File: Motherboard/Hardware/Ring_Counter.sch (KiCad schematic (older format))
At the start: 91 parts, among them Q10 BC848, Q11 BC848, Q12 BC848, Q13 BC848, Q14 BC848, Q15 BC848, Q16 BC848, Q17 BC858, Q18 BC848, Q19 BC858, Q20 BC848, Q21 BC858, Q22 BC858, Q23 BC848, Q24 BC848, Q25 BC848, Q26 BC848, Q27 BC848, Q28 BC848, Q29 BC848, Q30 BC848, Q31 BC848, Q32 BC848, Q33 BC848, Q34 BC858, Q35 BC858, Q36 BC858, Q37 BC858, Q38 BC858, Q39 BC858, Q40 BC848, Q41 BC848, Q42 BC858, Q43 BC858, Q46 BC858

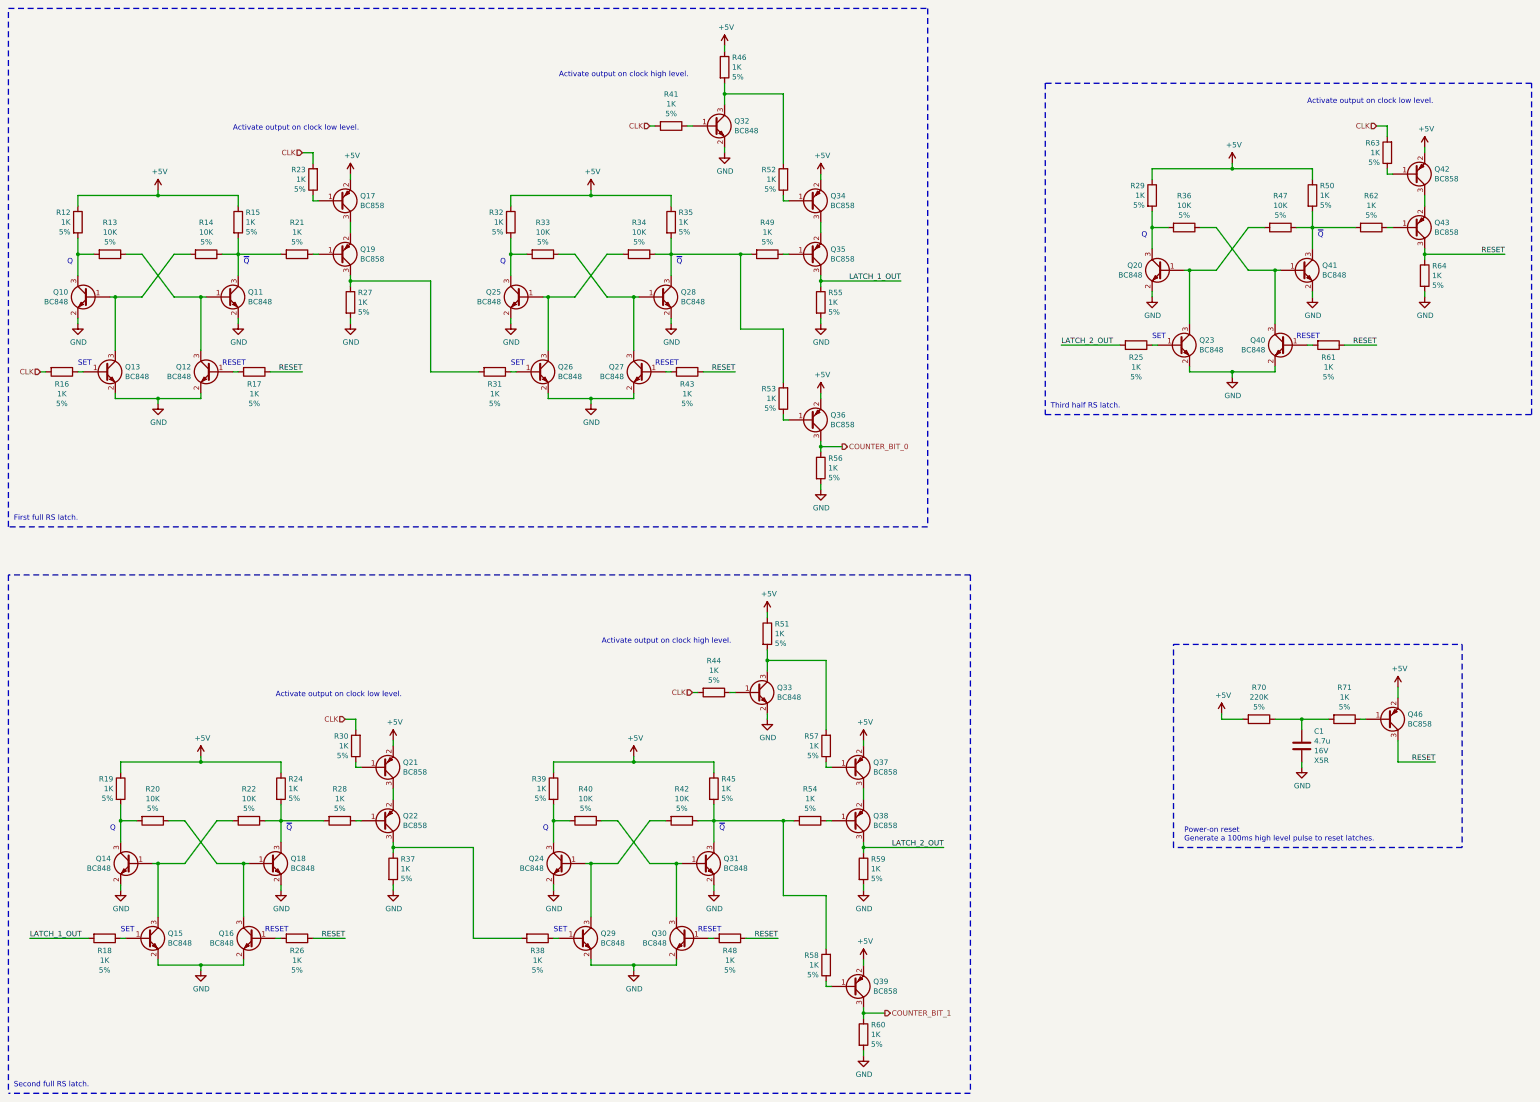
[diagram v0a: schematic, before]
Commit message: Renamed all motherboard components so the name are ordered.
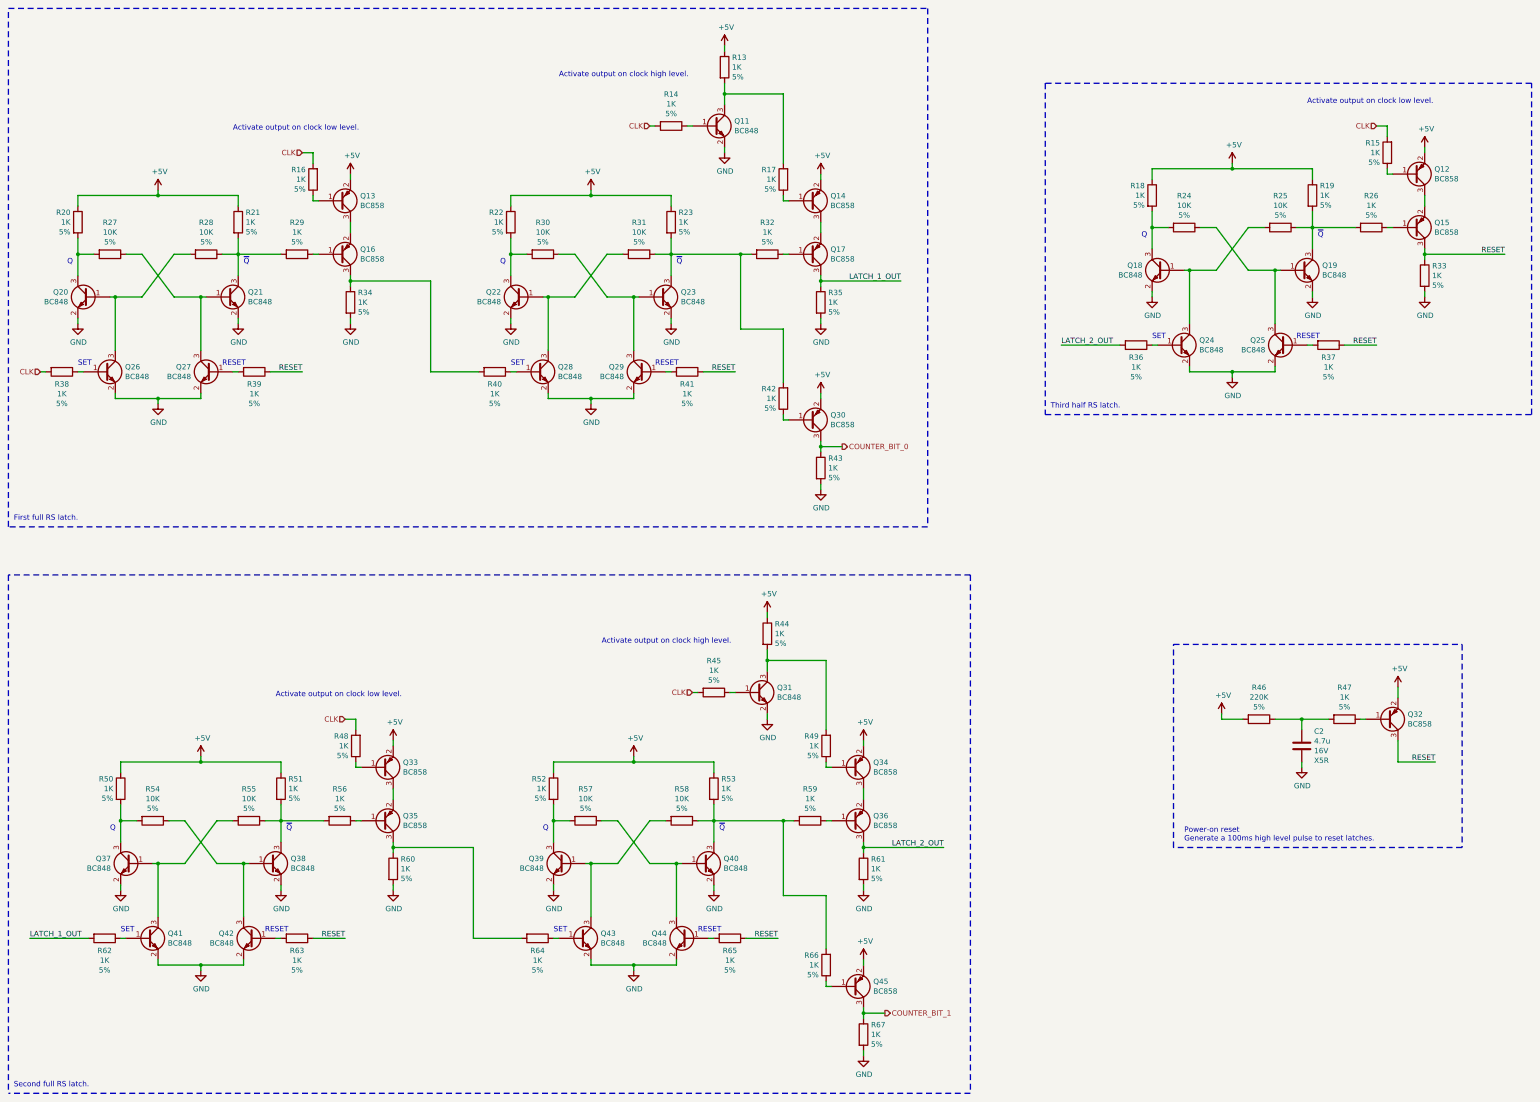
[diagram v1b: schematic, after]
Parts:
- renumbered C1 to C2, Q32 to Q11, Q42 to Q12, Q17 to Q13, Q34 to Q14, Q43 to Q15, Q19 to Q16, Q35 to Q17, Q20 to Q18, Q41 to Q19, Q10 to Q20, Q11 to Q21, Q25 to Q22, Q28 to Q23, Q23 to Q24, Q40 to Q25, Q13 to Q26, Q12 to Q27, Q26 to Q28, Q27 to Q29, Q36 to Q30, Q33 to Q31, Q46 to Q32, Q21 to Q33, Q37 to Q34, Q22 to Q35, Q38 to Q36, Q14 to Q37, Q18 to Q38, Q24 to Q39, Q31 to Q40, Q15 to Q41, Q16 to Q42, Q29 to Q43, Q30 to Q44, Q39 to Q45, R46 to R13, R41 to R14, R63 to R15, R23 to R16, R52 to R17, R29 to R18, R50 to R19, R12 to R20, R15 to R21, R32 to R22, R35 to R23, R36 to R24, R47 to R25, R62 to R26, R13 to R27, R14 to R28, R21 to R29, R33 to R30, R34 to R31, R49 to R32, R64 to R33, R27 to R34, R55 to R35, R25 to R36, R61 to R37, R16 to R38, R17 to R39, R31 to R40, R43 to R41, R53 to R42, R56 to R43, R51 to R44, R44 to R45, R70 to R46, R71 to R47, R30 to R48, R57 to R49, R19 to R50, R24 to R51, R39 to R52, R45 to R53, R20 to R54, R22 to R55, R28 to R56, R40 to R57, R42 to R58, R54 to R59, R37 to R60, R59 to R61, R18 to R62, R26 to R63, R38 to R64, R48 to R65, R58 to R66, R60 to R67

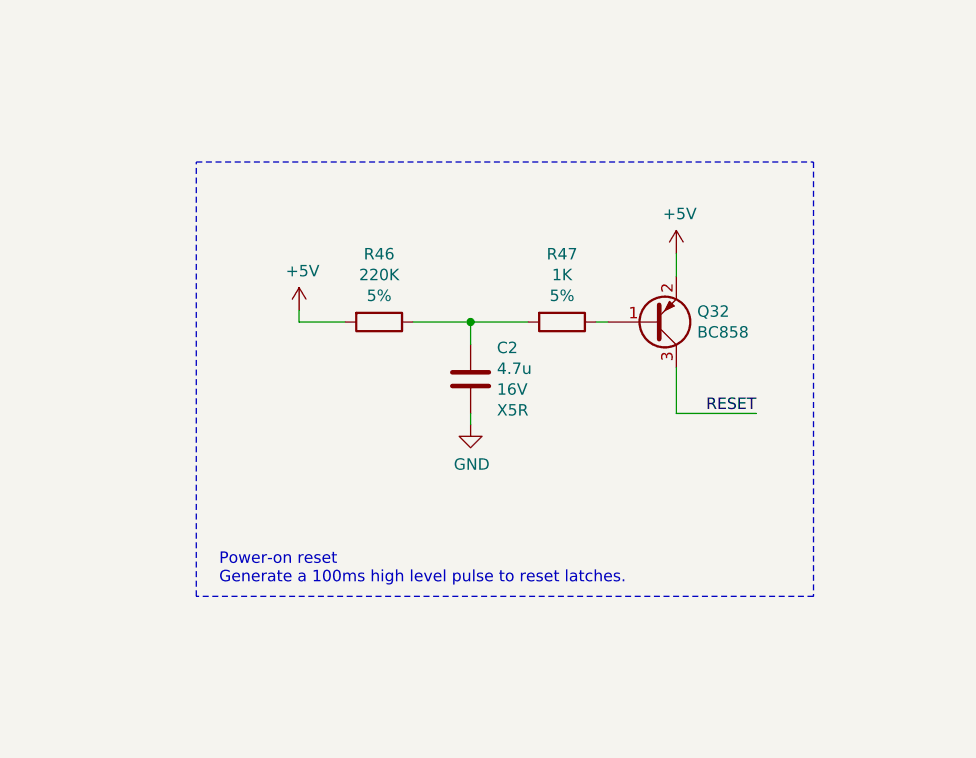
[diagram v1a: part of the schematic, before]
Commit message: Disabled the motherboard clock circuit power supply while power-on reset delay is running to avoid clocking the RS gates while they are being reset by the power-on reset.
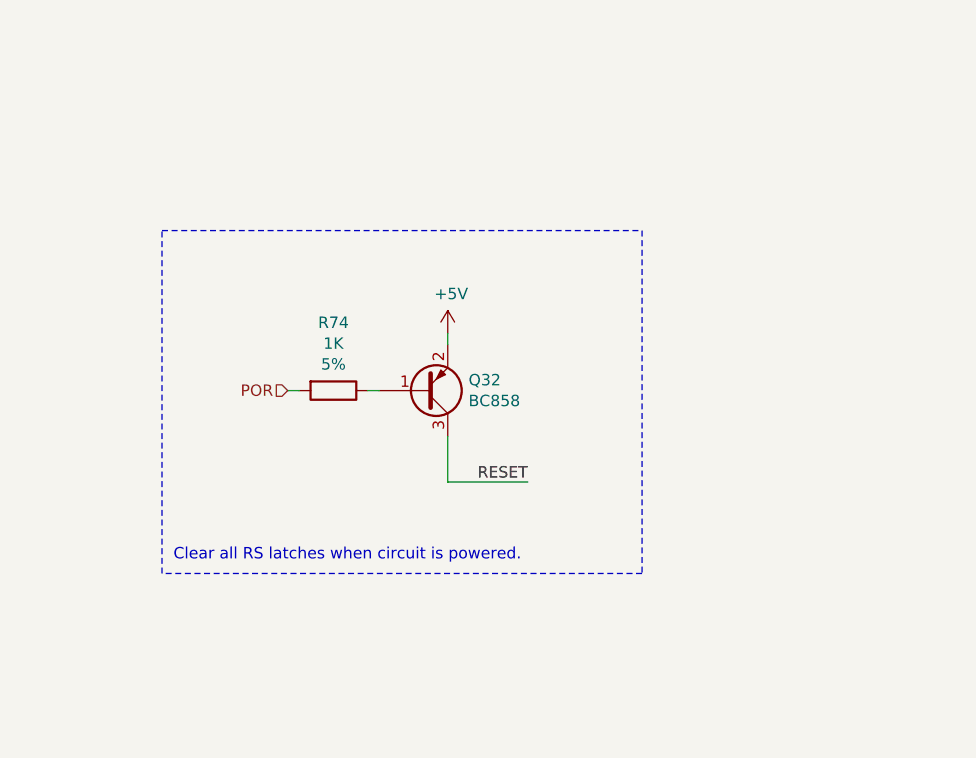
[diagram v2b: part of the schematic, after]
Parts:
- removed C2: 4.7u, Capacitor_SMD:C_0805_2012Metric_Pad1.18x1.45mm_HandSolder, symbol Device:C
- removed R46: 220K, Resistor_SMD:R_0603_1608Metric_Pad0.98x0.95mm_HandSolder, symbol Device:R
- removed R47: 1K, Resistor_SMD:R_0603_1608Metric_Pad0.98x0.95mm_HandSolder, symbol Device:R
- added R74: 1K, Resistor_SMD:R_0603_1608Metric_Pad0.98x0.95mm_HandSolder, symbol Device:R
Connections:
- net at Q32.1 (B): now also R74.1
- new net POR: R74.2
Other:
- note added: "Clear all RS latches when circuit is powered."
- note removed: "Power-on reset\nGenerate a 100ms high level pulse to reset latches."
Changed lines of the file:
@@
 Text Notes 10350 4500 0    50   ~ 0
 Third half RS latch.
-$Comp
-L Device:R R?
-U 1 1 6211682E
-P 12300 7400
-AR Path="/6211682E" Ref="R?"  Part="1"
-AR Path="/61D90E9A/6211682E" Ref="R46"  Part="1"
-F 0 "R46" V 12003 7400 50  0000 C CNN
-F 1 "220K" V 12094 7400 50  0000 C CNN
-F 2 "Resistor_SMD:R_0603_1608Metric_Pad0.98x0.95mm_HandSolder" V 12230 7400 50  0001 C CNN
-F 3 "~" H 12300 7400 50  0001 C CNN
-F 4 "5%" V 12185 7400 50  0000 C CNN "Value2"
-F 5 "R" H 12300 7400 50  0001 C CNN "Spice_Primitive"
-F 6 "1k" H 12300 7400 50  0001 C CNN "Spice_Model"
-F 7 "Y" H 12300 7400 50  0001 C CNN "Spice_Netlist_Enabled"
-	1    12300 7400
-	0    1    1    0
-$EndComp
-$Comp
-L Device:C C2
-U 1 1 62117E9F
-P 12700 7650
-F 0 "C2" H 12815 7787 50  0000 L CNN
-F 1 "4.7u" H 12815 7696 50  0000 L CNN
-F 2 "Capacitor_SMD:C_0805_2012Metric_Pad1.18x1.45mm_HandSolder" H 12738 7500 50  0001 C CNN
-F 3 "~" H 12700 7650 50  0001 C CNN
-F 4 "16V" H 12815 7605 50  0000 L CNN "Value2"
-F 5 "X5R" H 12815 7514 50  0000 L CNN "Value3"
-F 6 "CL21A475KOFNNNE" H 12700 7650 50  0001 C CNN "PartNumber"
-F 7 "Samsung" H 12700 7650 50  0001 C CNN "Manufacturer"
-	1    12700 7650
-	1    0    0    -1
-$EndComp
-$Comp
-L Device:R R?
-U 1 1 6211A796
-P 13100 7400
-AR Path="/6211A796" Ref="R?"  Part="1"
-AR Path="/61D90E9A/6211A796" Ref="R47"  Part="1"
-F 0 "R47" V 12803 7400 50  0000 C CNN
-F 1 "1K" V 12894 7400 50  0000 C CNN
-F 2 "Resistor_SMD:R_0603_1608Metric_Pad0.98x0.95mm_HandSolder" V 13030 7400 50  0001 C CNN
-F 3 "~" H 13100 7400 50  0001 C CNN
-F 4 "5%" V 12985 7400 50  0000 C CNN "Value2"
-F 5 "R" H 13100 7400 50  0001 C CNN "Spice_Primitive"
-F 6 "1k" H 13100 7400 50  0001 C CNN "Spice_Model"
-F 7 "Y" H 13100 7400 50  0001 C CNN "Spice_Netlist_Enabled"
-	1    13100 7400
-	0    1    1    0
-$EndComp
-$Comp
-L Transistor_BJT:BC858 Q32
-U 1 1 6211DBE2
-P 13500 7400
-F 0 "Q32" H 13691 7354 50  0000 L CNN
-F 1 "BC858" H 13691 7445 50  0000 L CNN
-F 2 "Package_TO_SOT_SMD:SOT-23" H 13700 7325 50  0001 L CIN
-F 3 "https://www.onsemi.com/pub/Collateral/BC860-D.pdf" H 13500 7400 50  0001 L CNN
-F 4 "Spice_Simulation/BC858.lib" H 13500 7400 50  0001 C CNN "Spice_Lib_File"
-F 5 "BC858" H 13500 7400 50  0001 C CNN "Spice_Model"
-F 6 "Y" H 13500 7400 50  0001 C CNN "Spice_Netlist_Enabled"
-F 7 "Q" H 13500 7400 50  0001 C CNN "Spice_Primitive"
-F 8 "3 1 2" H 13500 7400 50  0001 C CNN "Spice_Node_Sequence"
-	1    13500 7400
-	1    0    0    1
-$EndComp
-$Comp
-L power:+5V #PWR?
-U 1 1 6212D299
-P 13600 7100
-AR Path="/6212D299" Ref="#PWR?"  Part="1"
-AR Path="/61D90E9A/6212D299" Ref="#PWR041"  Part="1"
-F 0 "#PWR041" H 13600 6950 50  0001 C CNN
-F 1 "+5V" H 13615 7273 50  0000 C CNN
-F 2 "" H 13600 7100 50  0001 C CNN
-F 3 "" H 13600 7100 50  0001 C CNN
-F 4 "V" H 13600 7100 50  0001 C CNN "Spice_Primitive"
-F 5 "dc 5" H 13600 7100 50  0001 C CNN "Spice_Model"
-F 6 "Y" H 13600 7100 50  0001 C CNN "Spice_Netlist_Enabled"
-	1    13600 7100
-	1    0    0    -1
-$EndComp
-Text Label 13950 7800 2    50   ~ 0
-RESET
-Wire Wire Line
-	13600 7600 13600 7800
-Wire Wire Line
-	13600 7800 13950 7800
-Wire Wire Line
-	13250 7400 13300 7400
-Wire Wire Line
-	12450 7400 12700 7400
-Wire Wire Line
-	12700 7500 12700 7400
-Connection ~ 12700 7400
-Wire Wire Line
-	12700 7400 12950 7400
-Wire Wire Line
-	13600 7100 13600 7200
-$Comp
-L power:+5V #PWR?
-U 1 1 62180E8E
-P 11950 7350
-AR Path="/62180E8E" Ref="#PWR?"  Part="1"
-AR Path="/61D90E9A/62180E8E" Ref="#PWR042"  Part="1"
-F 0 "#PWR042" H 11950 7200 50  0001 C CNN
-F 1 "+5V" H 11965 7523 50  0000 C CNN
-F 2 "" H 11950 7350 50  0001 C CNN
-F 3 "" H 11950 7350 50  0001 C CNN
-F 4 "V" H 11950 7350 50  0001 C CNN "Spice_Primitive"
-F 5 "dc 5" H 11950 7350 50  0001 C CNN "Spice_Model"
-F 6 "Y" H 11950 7350 50  0001 C CNN "Spice_Netlist_Enabled"
-	1    11950 7350
-	1    0    0    -1
-$EndComp
-Wire Wire Line
-	11950 7400 12150 7400
-$Comp
-L power:GND #PWR048
-U 1 1 621A1546
-P 12700 7850
-F 0 "#PWR048" H 12700 7600 50  0001 C CNN
-F 1 "GND" H 12705 7677 50  0000 C CNN
-F 2 "" H 12700 7850 50  0001 C CNN
-F 3 "" H 12700 7850 50  0001 C CNN
-	1    12700 7850
-	1    0    0    -1
-$EndComp
-Wire Wire Line
-	12700 7800 12700 7850
-Wire Notes Line
-	11500 6700 14200 6700
-Wire Notes Line
-	14200 6700 14200 8600
-Wire Notes Line
-	14200 8600 11500 8600
-Wire Notes Line
-	11500 8600 11500 6700
-Text Notes 11600 8550 0    50   ~ 0
-Power-on reset\nGenerate a 100ms high level pulse to reset latches.
-Wire Wire Line
-	11950 7400 11950 7350
 Text HLabel 13400 1850 0    50   Input ~ 0
 CLK
@@
 Text HLabel 3350 2100 0    50   Input ~ 0
 CLK
+$Comp
+L Transistor_BJT:BC858 Q32
+U 1 1 621B3085
+P 12500 7700
+F 0 "Q32" H 12691 7654 50  0000 L CNN
+F 1 "BC858" H 12691 7745 50  0000 L CNN
+F 2 "Package_TO_SOT_SMD:SOT-23" H 12700 7625 50  0001 L CIN
+F 3 "https://www.onsemi.com/pub/Collateral/BC860-D.pdf" H 12500 7700 50  0001 L CNN
+F 4 "Spice_Simulation/BC858.lib" H 12500 7700 50  0001 C CNN "Spice_Lib_File"
+F 5 "BC858" H 12500 7700 50  0001 C CNN "Spice_Model"
+F 6 "Y" H 12500 7700 50  0001 C CNN "Spice_Netlist_Enabled"
+F 7 "Q" H 12500 7700 50  0001 C CNN "Spice_Primitive"
+F 8 "3 1 2" H 12500 7700 50  0001 C CNN "Spice_Node_Sequence"
+	1    12500 7700
+	1    0    0    1
+$EndComp
+$Comp
+L power:+5V #PWR?
+U 1 1 621B308E
+P 12600 7450
+AR Path="/621B308E" Ref="#PWR?"  Part="1"
+AR Path="/61D90E9A/621B308E" Ref="#PWR041"  Part="1"
+F 0 "#PWR041" H 12600 7300 50  0001 C CNN
+F 1 "+5V" H 12615 7623 50  0000 C CNN
+F 2 "" H 12600 7450 50  0001 C CNN
+F 3 "" H 12600 7450 50  0001 C CNN
+F 4 "V" H 12600 7450 50  0001 C CNN "Spice_Primitive"
+F 5 "dc 5" H 12600 7450 50  0001 C CNN "Spice_Model"
+F 6 "Y" H 12600 7450 50  0001 C CNN "Spice_Netlist_Enabled"
+	1    12600 7450
+	1    0    0    -1
+$EndComp
+Text Label 12950 8100 2    50   ~ 0
+RESET
+Wire Wire Line
+	12600 7900 12600 8100
+Wire Wire Line
+	12600 8100 12950 8100
+Wire Wire Line
+	12600 7450 12600 7500
+Text HLabel 11900 7700 0    50   Input ~ 0
+POR
+Wire Wire Line
+	12300 7700 12250 7700
+Wire Notes Line
+	13450 7000 13450 8500
+Wire Notes Line
+	13450 8500 11350 8500
+Wire Notes Line
+	11350 8500 11350 7000
+Wire Notes Line
+	11350 7000 13450 7000
+Text Notes 11400 8450 0    50   ~ 0
+Clear all RS latches when circuit is powered.
+$Comp
+L Device:R R?
+U 1 1 6227A007
+P 12100 7700
+AR Path="/6227A007" Ref="R?"  Part="1"
+AR Path="/61D90E9A/6227A007" Ref="R74"  Part="1"
+AR Path="/622B55AD/6227A007" Ref="R?"  Part="1"
+F 0 "R74" V 11803 7700 50  0000 C CNN
+F 1 "1K" V 11894 7700 50  0000 C CNN
+F 2 "Resistor_SMD:R_0603_1608Metric_Pad0.98x0.95mm_HandSolder" V 12030 7700 50  0001 C CNN
+F 3 "~" H 12100 7700 50  0001 C CNN
+F 4 "5%" V 11985 7700 50  0000 C CNN "Value2"
+F 5 "R" H 12100 7700 50  0001 C CNN "Spice_Primitive"
+F 6 "1k" H 12100 7700 50  0001 C CNN "Spice_Model"
+F 7 "Y" H 12100 7700 50  0001 C CNN "Spice_Netlist_Enabled"
+	1    12100 7700
+	0    1    1    0
+$EndComp
+Wire Wire Line
+	11900 7700 11950 7700
 $EndSCHEMATC
